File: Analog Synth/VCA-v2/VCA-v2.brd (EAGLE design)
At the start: 67.3 x 100 mm, 44 parts, among them IC2 TL084D, T1 2N3904, T2 2N3904, T3 2N3904

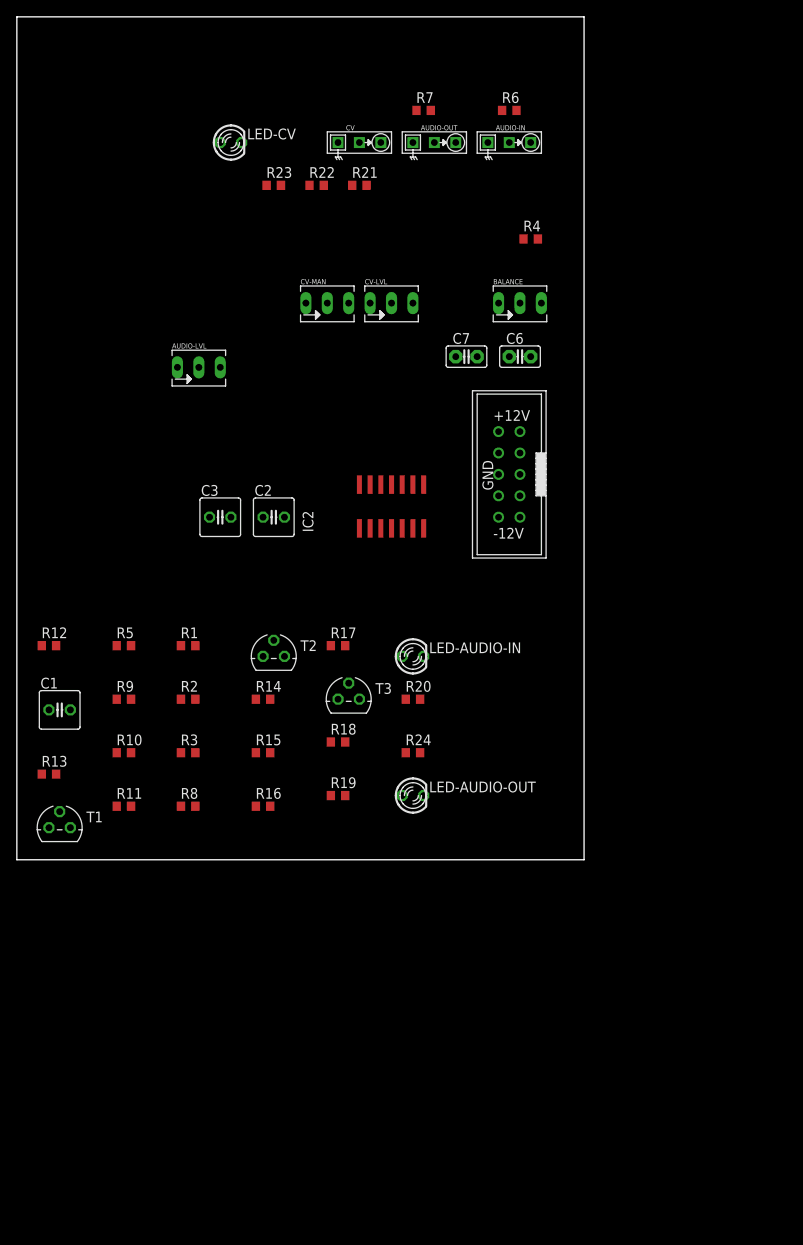
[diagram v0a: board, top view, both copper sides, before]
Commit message: added DMMT3904W to part library in synth_sch; making progress on VCA-v2 layout
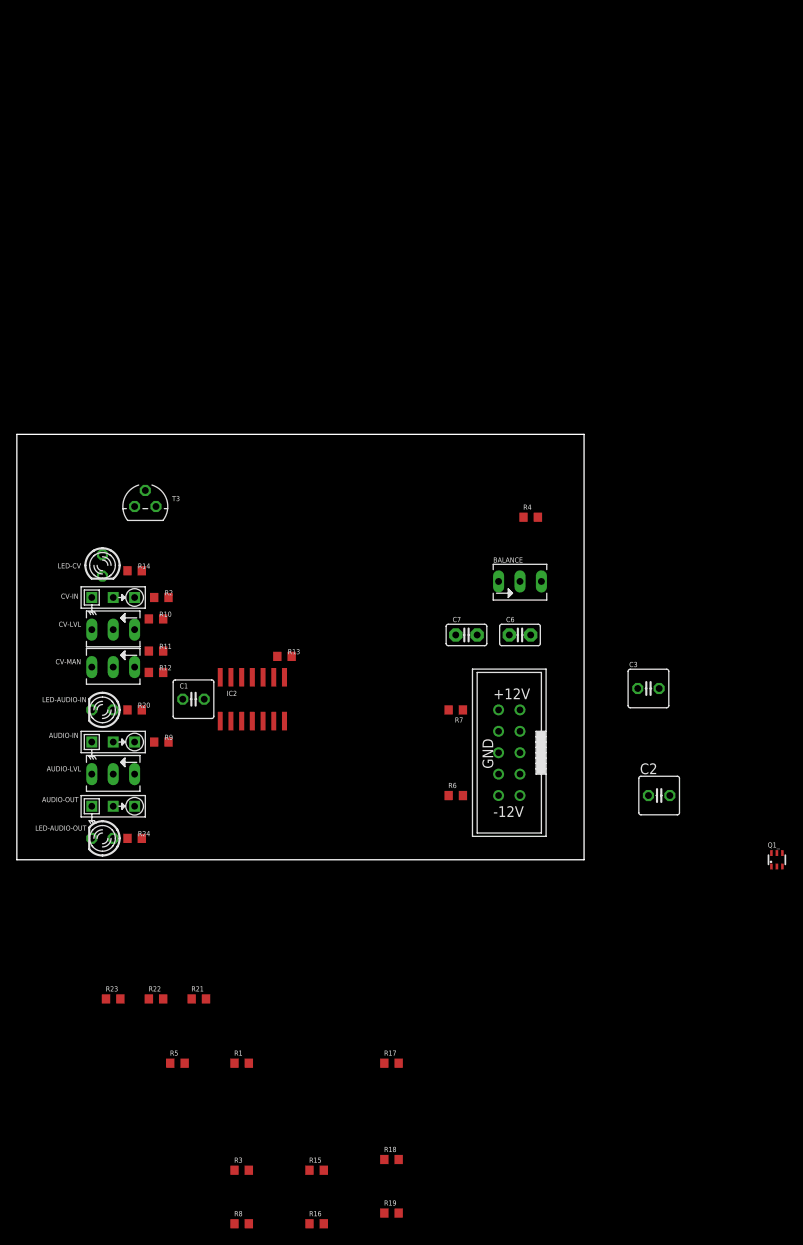
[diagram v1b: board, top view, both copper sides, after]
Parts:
- removed CV: I/O, !synth_sch:MONO_JACK
- removed T1, T2: 2N3904, transistor-neu-to92:TO92
- added CV-IN: I/O, !synth_sch:MONO_JACK
- added Q1_: DMMT3904W, !synth_sch:SOT363
- moved R21 98.4 mm to (21.6, -16.5)
- moved R22 98.4 mm to (16.5, -16.5)
- moved R23 98.4 mm to (11.4, -16.5)
- moved AUDIO-OUT 87.5 mm to (11.4, 6.35)
- moved AUDIO-IN 85.2 mm to (11.4, 14.0)
- moved R6 81.5 mm to (52.1, 7.62)
- moved R7 71.2 mm to (52.1, 17.8), turned to 180 degrees
- moved C2 56.4 mm to (76.2, 7.62)
- moved C3 54.7 mm to (74.9, 20.3)
- moved LED-CV 52.4 mm to (10.2, 34.9), turned to 270 degrees
- moved CV-LVL 50.9 mm to (11.4, 27.3), turned to 180 degrees
- moved CV-MAN 50.1 mm to (11.4, 22.9), turned to 180 degrees
- moved R1 49.9 mm to (26.7, -24.1)
- moved R15 49.9 mm to (35.6, -36.8)
- moved R16 49.9 mm to (35.6, -43.2)
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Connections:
- removed net N$23: LED-AUDIO-OUT.K, R24.2
- new net N$22: LED-AUDIO-OUT.A, R24.1
- net GND: now also CV-IN.P$1, CV-IN.P$3, IC2.10, LED-AUDIO-IN.K, LED-AUDIO-OUT.K; no longer CV.P$1, CV.P$3, IC2.5, R20.1, R24.1
- net N$1: now also IC2.8; no longer IC2.7
- net N$15: now also Q1_.4, Q1_.5; no longer T1.3, T2.3
- net N$16: now also Q1_.1; no longer T1.2
- net N$17: now also IC2.9; no longer IC2.6
- net N$19: now also Q1_.2; no longer T2.2
- net N$21: now also LED-AUDIO-IN.A, R20.1; no longer LED-AUDIO-IN.K, R20.2
- net N$24: now also Q1_.6; no longer T1.1
- net N$26: now also Q1_.3; no longer T2.1
- net N$28: now also IC2.5; no longer IC2.10
- net N$3: now also IC2.12; no longer IC2.3
- net N$30: now also IC2.6; no longer IC2.9
- net N$31: now also IC2.7, R24.2; no longer IC2.8, LED-AUDIO-OUT.A
- net N$32: no longer AUDIO-OUT.P$3
- net N$4: now also IC2.13, IC2.14; no longer IC2.1, IC2.2
- net N$5: now also CV-IN.P$2; no longer CV.P$2
- net N$7: now also IC2.3; no longer IC2.12
- net N$9: now also IC2.1, IC2.2, R20.2; no longer IC2.13, IC2.14, LED-AUDIO-IN.A
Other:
- board size 67.3 x 100 mm -> 67.3 x 50.5 mm

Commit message: making progress on VCA-v2. Updated the Eurorack power connector
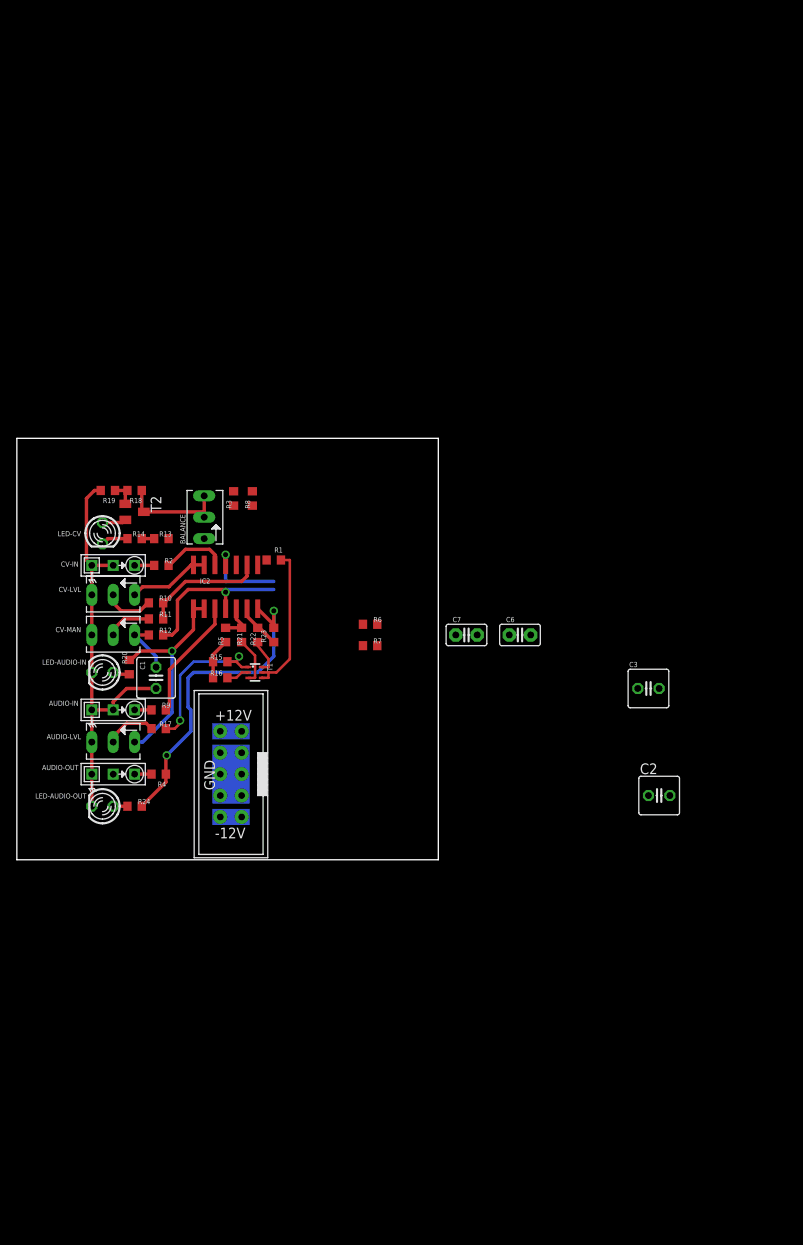
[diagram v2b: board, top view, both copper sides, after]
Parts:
- removed Q1_: DMMT3904W, !synth_sch:SOT363
- removed T3: 2N3904, transistor-neu-to92:TO92
- added T1: DMMT3904W, !synth_sch:SOT363
- added T2: MMBT2222ALT1, transistor:SOT23-BEC
- moved R19 92.1 mm to (10.8, 43.8), turned to 180 degrees
- moved R8 86.1 mm to (27.9, 42.9), turned to 90 degrees
- moved R18 85.0 mm to (14.0, 43.8), turned to 180 degrees
- moved R3 79.7 mm to (25.7, 42.9), turned to 90 degrees
- moved R16 65.8 mm to (24.1, 21.6)
- moved R15 61.4 mm to (24.1, 23.5)
- moved R1 59.8 mm to (30.5, 35.6)
- moved R4 53.6 mm to (16.8, 10.2), turned to 180 degrees
- moved R5 51.1 mm to (24.8, 26.7), turned to 90 degrees
- moved R17 48.4 mm to (16.8, 15.6)
- moved R23 47.2 mm to (30.5, 26.7), turned to 90 degrees
- moved R22 44.8 mm to (28.6, 26.7), turned to 90 degrees
- moved R21 43.5 mm to (26.7, 26.7), turned to 90 degrees
- moved BALANCE 38.2 mm to (22.2, 40.6), turned to 90 degrees
- moved U$1 33.1 mm to (25.4, 10.2)
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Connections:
- net +12V: now also T2.C; no longer T3.1
- net LED_SUPPLY: now also T2.E; no longer T3.3
- net N$15: now also T1.4, T1.5; no longer Q1_.4, Q1_.5
- net N$16: now also T1.1; no longer Q1_.1
- net N$19: now also T1.2; no longer Q1_.2
- net N$20: now also T2.B; no longer T3.2
- net N$24: now also T1.6; no longer Q1_.6
- net N$26: now also T1.3; no longer Q1_.3
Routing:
- net GND: track 0.00 -> 55.5 mm
- net N$31: track 0.00 -> 39.5 mm, vias 0 -> 2
- net +12V: track 0.00 -> 32.3 mm, vias 0 -> 1
- net N$9: track 0.00 -> 26.4 mm, vias 0 -> 1
- net N$16: track 0.00 -> 19.3 mm, vias 0 -> 2
- net N$15: track 0.00 -> 18.2 mm
- net N$17: track 0.00 -> 14.5 mm
- net N$7: track 0.00 -> 14.4 mm
- net -12V: track 0.00 -> 10.1 mm, vias 0 -> 1
- net N$4: track 0.00 -> 9.71 mm
- net N$3: track 0.00 -> 7.76 mm
- net N$14: track 0.00 -> 6.55 mm
- net N$18: track 0.00 -> 6.10 mm
- net N$11: track 0.00 -> 6.09 mm
- net N$26: track 0.00 -> 5.69 mm
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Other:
- board size 67.3 x 50.5 mm -> 50 x 50 mm

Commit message: making some progress on VCA-v2
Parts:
- C6, C7: device capacitor-wima:C2.5-2 -> rcl:C0603
- moved C2 63.0 mm to (13.3, 2.86), turned to 270 degrees
- moved C3 59.5 mm to (18.1, 2.86), turned to 270 degrees
- moved C6 31.9 mm to (31.1, 12.4), turned to 270 degrees
- moved C7 28.9 mm to (31.1, 8.26), turned to 270 degrees
- moved R6 25.6 mm to (31.1, 4.76), turned to 270 degrees
- moved R7 14.2 mm to (31.1, 16.2), turned to 90 degrees
- moved R24 3.27 mm to (16.8, 7.94)
- moved LED-AUDIO-OUT 0.32 mm to (10.2, 6.67)
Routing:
- net -12V: track 10.1 -> 63.8 mm, vias 1 -> 2
- net +12V: track 32.3 -> 85.2 mm, vias 1 -> 2
- net GND: track 55.5 -> 95.8 mm
- net N$10: track 0.00 -> 7.03 mm
- net N$8: track 0.00 -> 5.01 mm
- net N$22: track 1.69 -> 4.72 mm
- net N$31: track 39.5 -> 36.7 mm
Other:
- board size 50 x 50 mm -> 36 x 46.2 mm
